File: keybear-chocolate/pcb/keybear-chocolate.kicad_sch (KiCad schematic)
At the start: 102 parts, among them J1 MJ-4PP-9, J2 BATT, J3 LED, J4 OLED, SW1 SW_PUSH, SW10 SW_PUSH, SW11 SW_PUSH, SW12 SW_PUSH, SW13 SW_PUSH, SW14 SW_PUSH, SW15 SW_PUSH, SW16 SW_PUSH, SW17 SW_PUSH, SW18 SW_PUSH, SW19 SW_PUSH, SW2 SW_PUSH, SW20 SW_PUSH, SW21 SW_PUSH, SW22 SW_PUSH, SW25 Rotary_Encoder_Switch, SW3 SW_PUSH, SW30 BATT_SW, SW4 SW_PUSH, SW5 SW_PUSH, SW6 SW_PUSH, SW7 SW_PUSH, SW8 SW_PUSH, SW9 SW_PUSH, U1 ProMicro

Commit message: usb-c added - WIP
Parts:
- added P1: USB_C_Plug, Connector_USB:USB_C_Receptacle_G-Switch_GT-USB-7010ASV, symbol Connector:USB_C_Receptacle
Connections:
- net GND: now also P1.A1 (GND), P1.A12 (GND), P1.B1 (GND), P1.B12 (GND)
- net VCC: now also P1.A4 (VBUS), P1.A9 (VBUS), P1.B4 (VBUS), P1.B9 (VBUS)
- net at J1.B, JP12.2, JP14.2: now also P1.A7 (D-), P1.B7 (D-)
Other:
- moved on the sheet: J1, J3, JP12, JP13, L1, L10, L11, L12, L13, L14, L15, L16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

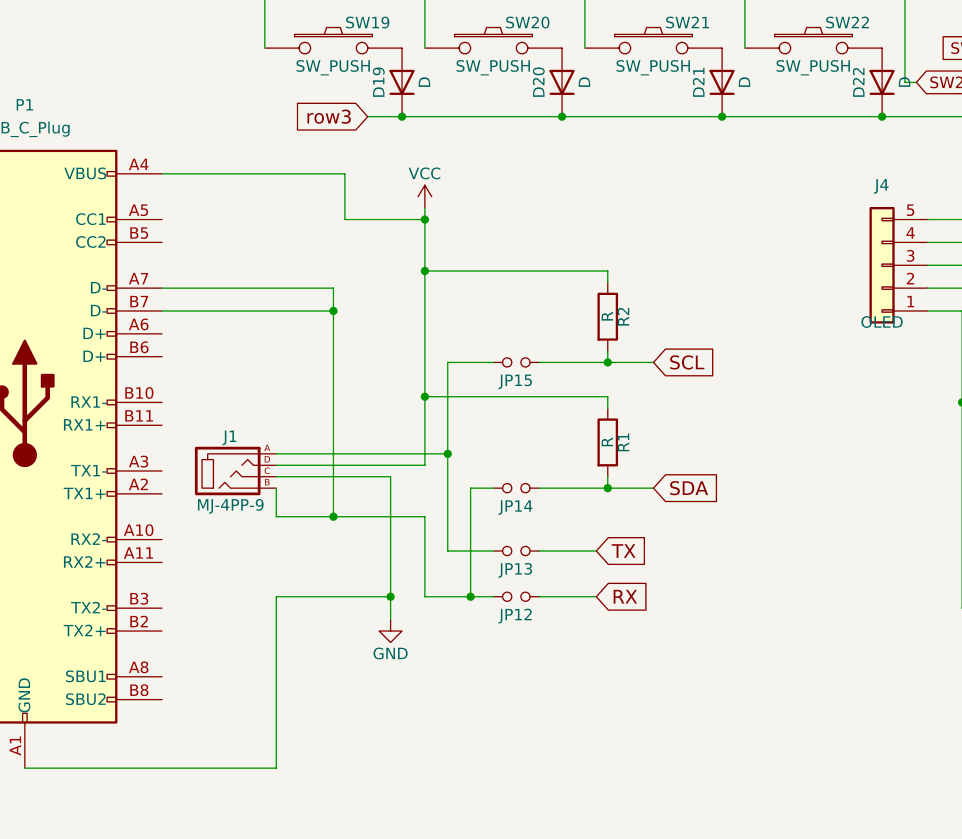
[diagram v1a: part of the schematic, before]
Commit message: usb-c rx-tx connections added
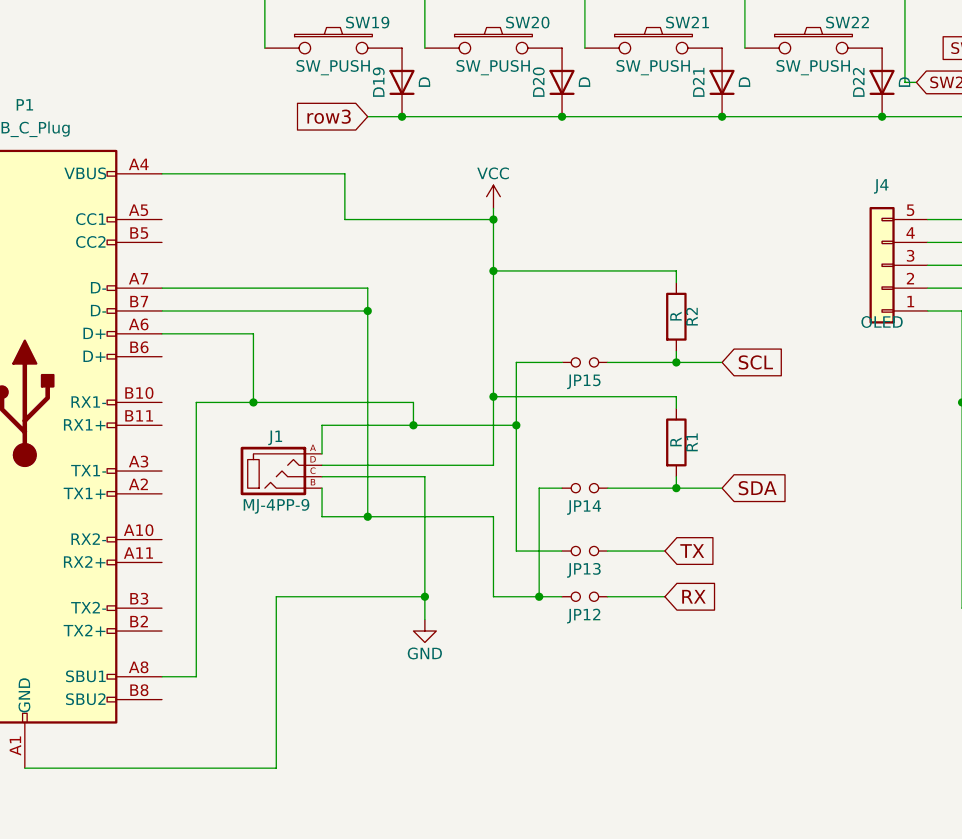
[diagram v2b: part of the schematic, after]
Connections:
- net at J1.A, JP13.2, JP15.2: now also P1.A6 (D+), P1.A8 (SBU1)
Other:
- moved on the sheet: J1, JP12, JP13, JP14, JP15, R1, R2

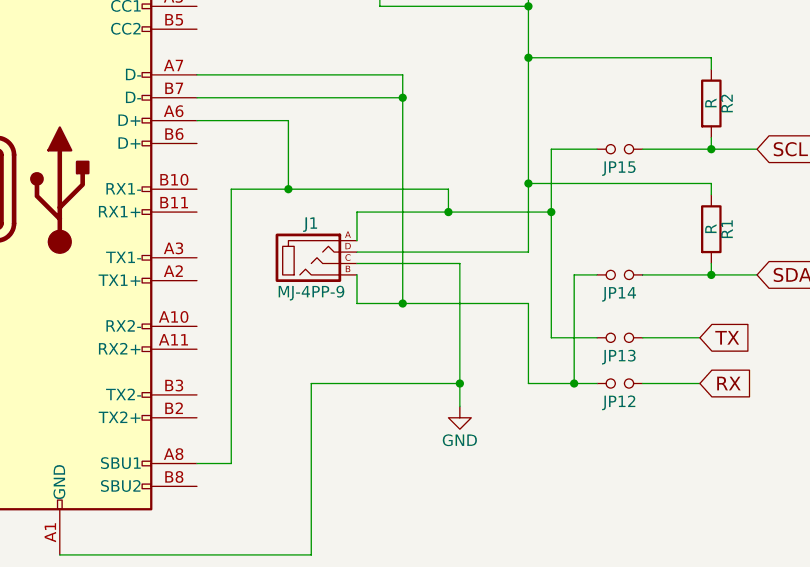
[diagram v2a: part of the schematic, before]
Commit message: trrs deleted. usb-c connected - v0.5
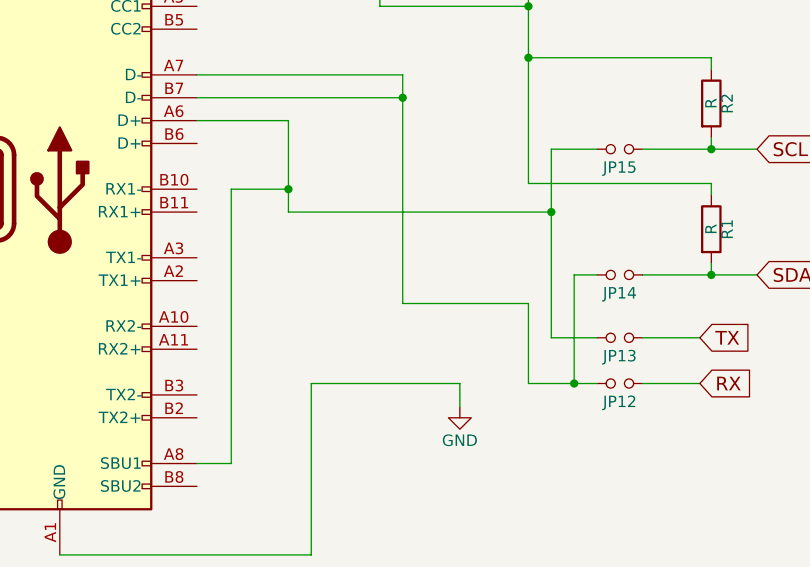
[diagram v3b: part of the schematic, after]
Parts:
- removed J1: MJ-4PP-9, kbd:MJ-4PP-9, symbol corne-chocolate-rescue:MJ-4PP-9-kbd
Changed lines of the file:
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@@
   (junction (at 232.41 58.42) (diameter 0) (color 0 0 0 0)
   )
-  (junction (at 181.61 157.48) (diameter 0) (color 0 0 0 0)
-  )
   (junction (at 217.17 81.28) (diameter 0) (color 0 0 0 0)
   )
@@
   (junction (at 49.53 167.64) (diameter 0) (color 0 0 0 0)
   )
-  (junction (at 180.34 138.43) (diameter 0) (color 0 0 0 0)
-  )
   (junction (at 34.29 172.72) (diameter 0) (color 0 0 0 0)
   )
-  (junction (at 175.26 148.59) (diameter 0) (color 0 0 0 0)
-  )
   (junction (at 234.95 66.04) (diameter 0) (color 0 0 0 0)
   )
@@
   (junction (at 250.19 73.66) (diameter 0) (color 0 0 0 0)
   )
-  (junction (at 189.23 135.255) (diameter 0) (color 0 0 0 0)
-  )
   (junction (at 64.77 172.72) (diameter 0) (color 0 0 0 0)
   )
@@
   (no_connect (at 121.92 64.77))
   (no_connect (at 31.75 172.72))
-  (wire (pts (xy 170.18 138.43) (xy 180.34 138.43))
-    (stroke (width 0) (type default))
-  )
   (wire (pts (xy 217.17 66.04) (xy 217.17 81.28))
     (stroke (width 0) (type default))
@@
     (stroke (width 0) (type default))
   )
-  (wire (pts (xy 170.18 138.43) (xy 170.18 141.605))
-    (stroke (width 0) (type default))
-  )
   (wire (pts (xy 209.55 144.145) (xy 209.55 145.415))
     (stroke (width 0) (type default))
@@
     (stroke (width 0) (type default))
   )
-  (wire (pts (xy 180.34 138.43) (xy 191.77 138.43))
-    (stroke (width 0) (type default))
-  )
   (wire (pts (xy 110.49 167.64) (xy 110.49 180.34))
     (stroke (width 0) (type default))
@@
     (stroke (width 0) (type default))
   )
-  (wire (pts (xy 170.18 144.145) (xy 181.61 144.145))
-    (stroke (width 0) (type default))
-  )
   (wire (pts (xy 242.57 123.19) (xy 237.49 123.19))
     (stroke (width 0) (type default))
@@
     (stroke (width 0) (type default))
   )
-  (wire (pts (xy 170.18 142.875) (xy 189.23 142.875))
-    (stroke (width 0) (type default))
-  )
   (wire (pts (xy 194.31 145.415) (xy 194.31 157.48))
     (stroke (width 0) (type default))
@@
     (stroke (width 0) (type default))
   )
-  (wire (pts (xy 180.34 135.89) (xy 180.34 138.43))
-    (stroke (width 0) (type default))
-  )
   (wire (pts (xy 80.01 154.94) (xy 80.01 160.02))
     (stroke (width 0) (type default))
@@
     (stroke (width 0) (type default))
   )
-  (wire (pts (xy 170.18 148.59) (xy 170.18 145.415))
+  (wire (pts (xy 62.23 189.23) (xy 46.99 189.23))
     (stroke (width 0) (type default))
   )
-  (wire (pts (xy 62.23 189.23) (xy 46.99 189.23))
+  (wire (pts (xy 162.56 138.43) (xy 162.56 135.89))
     (stroke (width 0) (type default))
   )
@@
     (stroke (width 0) (type default))
   )
-  (wire (pts (xy 162.56 135.89) (xy 180.34 135.89))
+  (wire (pts (xy 162.56 138.43) (xy 191.77 138.43))
     (stroke (width 0) (type default))
   )
@@
     (stroke (width 0) (type default))
   )
-  (wire (pts (xy 175.26 148.59) (xy 170.18 148.59))
-    (stroke (width 0) (type default))
-  )
   (wire (pts (xy 20.955 109.855) (xy 29.21 109.855))
     (stroke (width 0) (type default))
@@
     (stroke (width 0) (type default))
   )
-  (wire (pts (xy 181.61 144.145) (xy 181.61 157.48))
-    (stroke (width 0) (type default))
-  )
   (wire (pts (xy 49.53 142.24) (xy 49.53 147.32))
     (stroke (width 0) (type default))
@@
     (stroke (width 0) (type default))
   )
-  (wire (pts (xy 189.23 142.875) (xy 189.23 135.255))
-    (stroke (width 0) (type default))
-  )
   (wire (pts (xy 62.23 180.34) (xy 64.77 180.34))
     (stroke (width 0) (type default))
@@
         )
       )
-    )
-  )
-  (symbol (lib_id "corne-chocolate-rescue:MJ-4PP-9-kbd") (at 165.1 143.51 0) (unit 1)
-    (in_bom yes) (on_board yes) (dnp no)
-    (property "Reference" "J1" (at 165.1 139.7 0)
-      (effects (font (size 1.27 1.27)))
-    )
-    (property "Value" "MJ-4PP-9" (at 165.1 147.32 0)
-      (effects (font (size 1.27 1.27)))
-    )
-    (property "Footprint" "kbd:MJ-4PP-9" (at 172.085 139.065 0)
-      (effects (font (size 1.27 1.27)) hide)
-    )
-    (property "Datasheet" "" (at 172.085 139.065 0)
-      (effects (font (size 1.27 1.27)) hide)
-    )
-    (pin "A")
-    (pin "B")
-    (pin "C")
-    (pin "D")
-    (instances
-      (project "keybear-chocolate"
-        (path "/b2404ab0-025a-473e-9fbb-0abc932972cf"
-          (reference "J1") (unit 1)
-        )
-      )

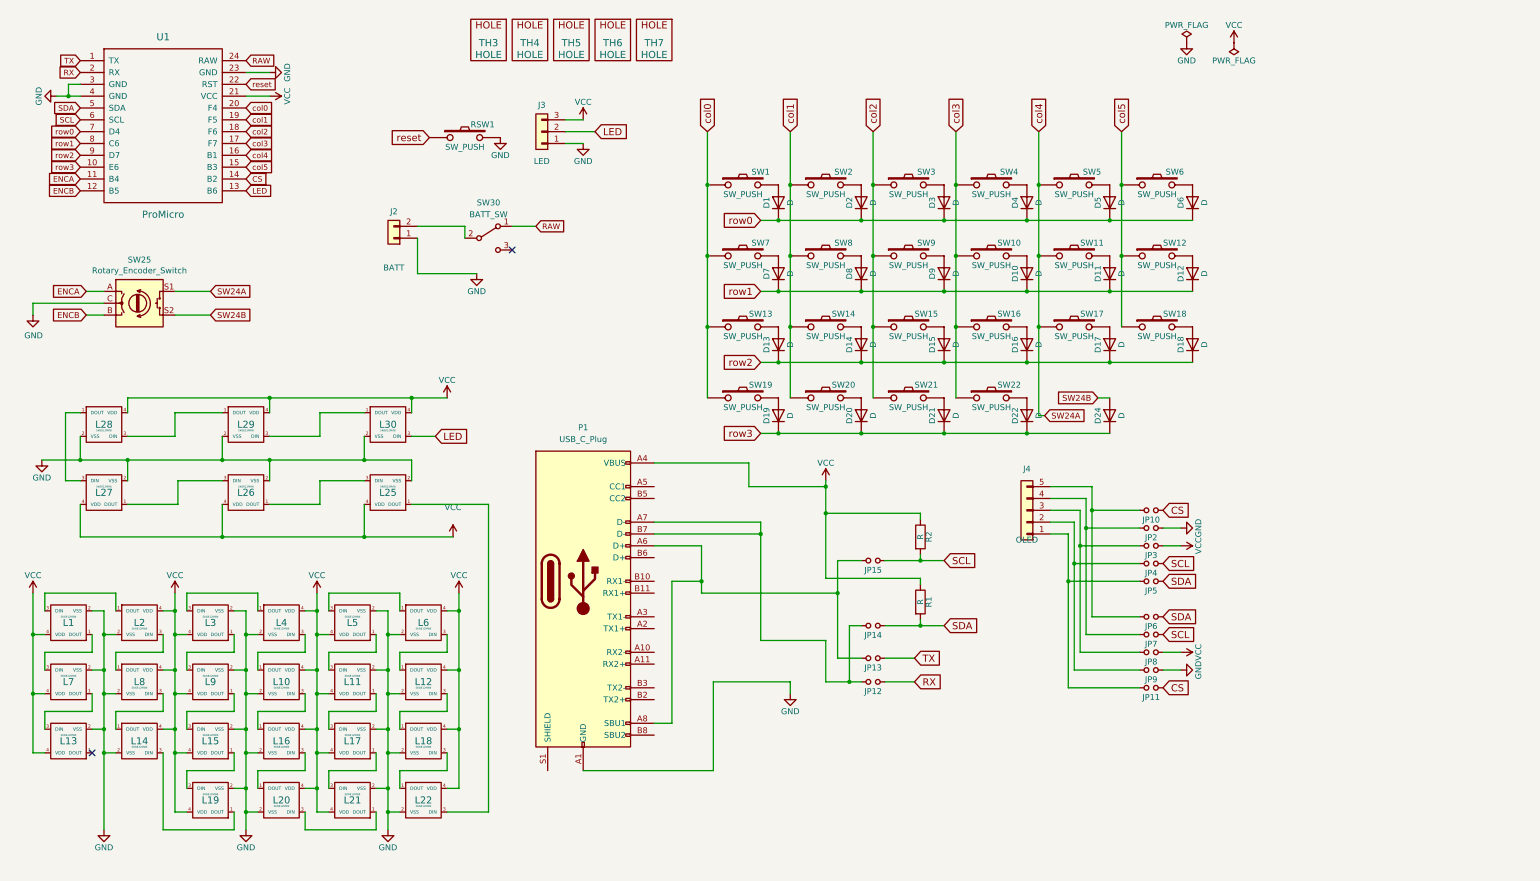
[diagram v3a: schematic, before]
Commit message: adding MPC23P17_ML to add the external GPIO pins
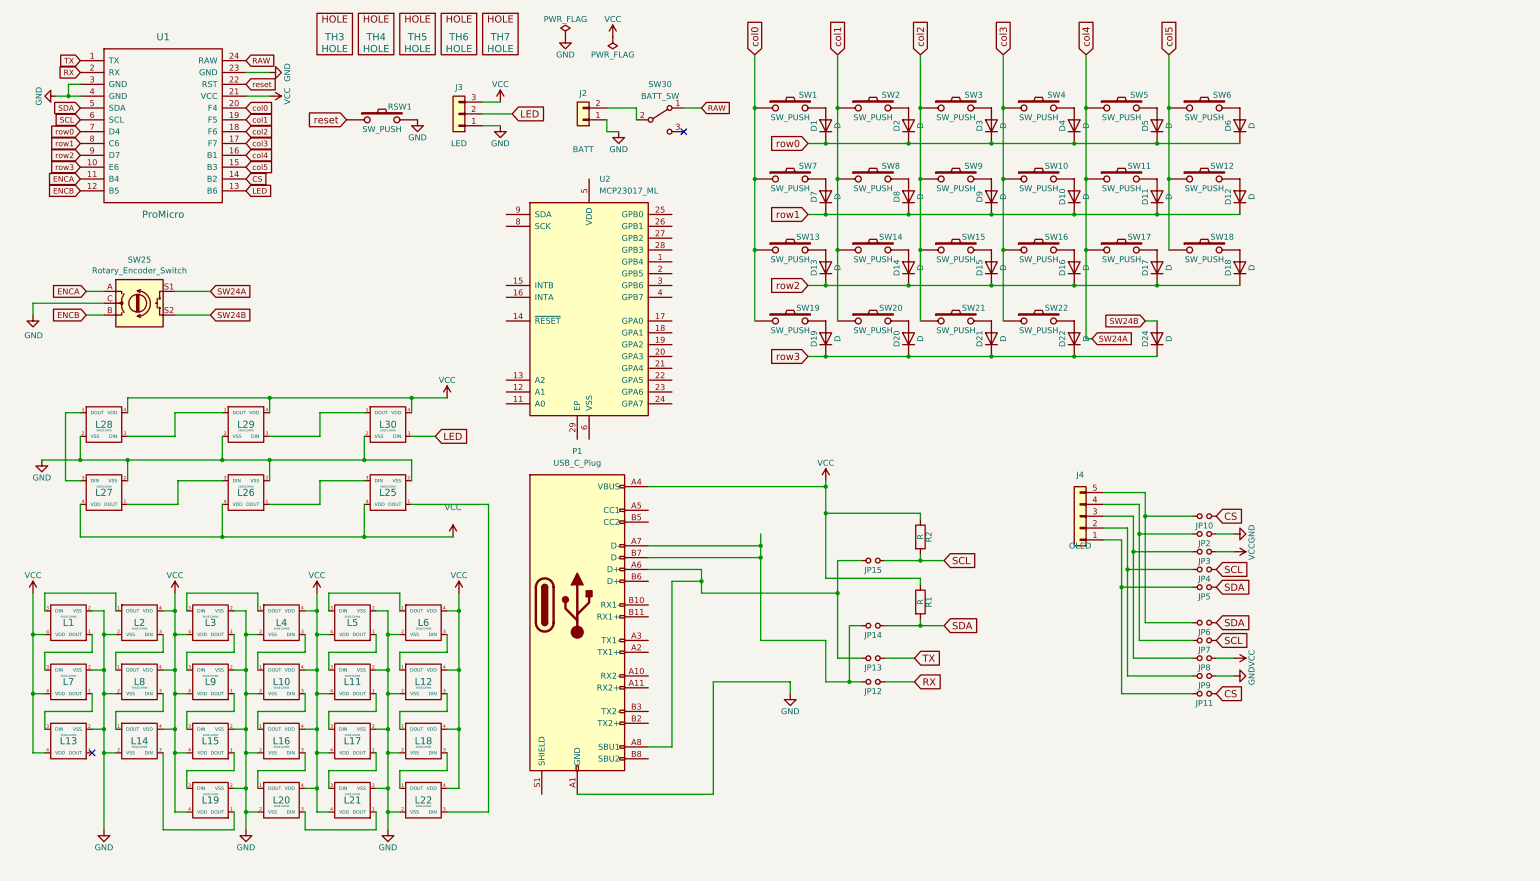
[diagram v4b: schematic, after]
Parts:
- added U2: MCP23017_ML, Package_DFN_QFN:QFN-28-1EP_6x6mm_P0.65mm_EP4.25x4.25mm, symbol Interface_Expansion:MCP23017_ML
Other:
- moved on the sheet: D1, D10, D11, D12, D13, D14, D15, D16, D17, D18, D19, D2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

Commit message: connecting MPC23P17_ML
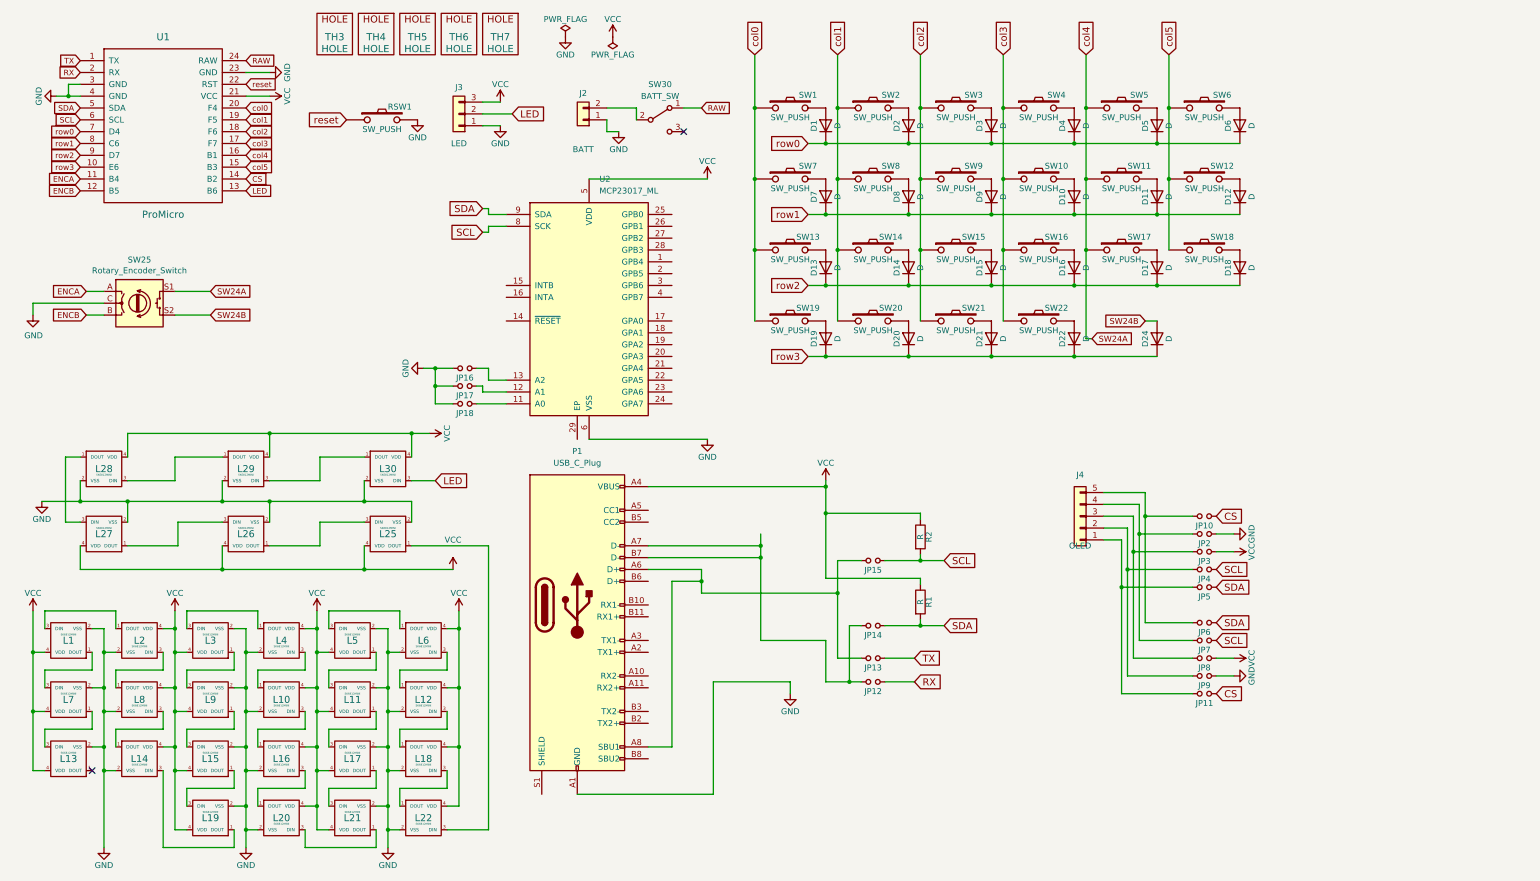
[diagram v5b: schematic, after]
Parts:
- added JP16, JP17, JP18: (no value), kbd:Jumper, symbol corne-chocolate-rescue:Jumper_NO_Small-Device
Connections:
- net GND: now also U2.6 (VSS), JP16.2, JP17.2, JP18.2
- net SCL: now also U2.8 (SCK)
- net SDA: now also U2.9 (SDA)
- net VCC: now also U2.5 (VDD)
- net at U2.11 (A0): now also JP18.1
- net at U2.12 (A1): now also JP17.1
- net at U2.13 (A2): now also JP16.1
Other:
- moved on the sheet: L1, L10, L11, L12, L13, L14, L15, L16, L17, L18, L19, L2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

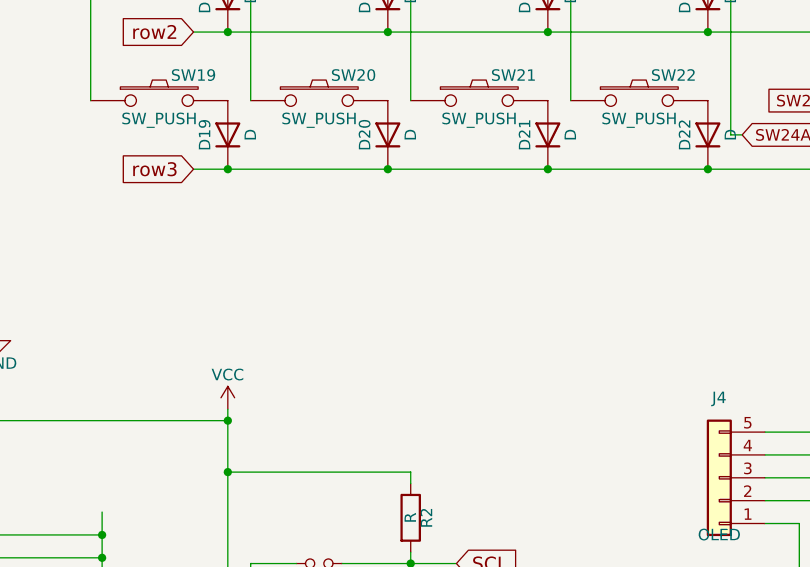
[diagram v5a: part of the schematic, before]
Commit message: adding ATECC608A-SSHDA crypto chip
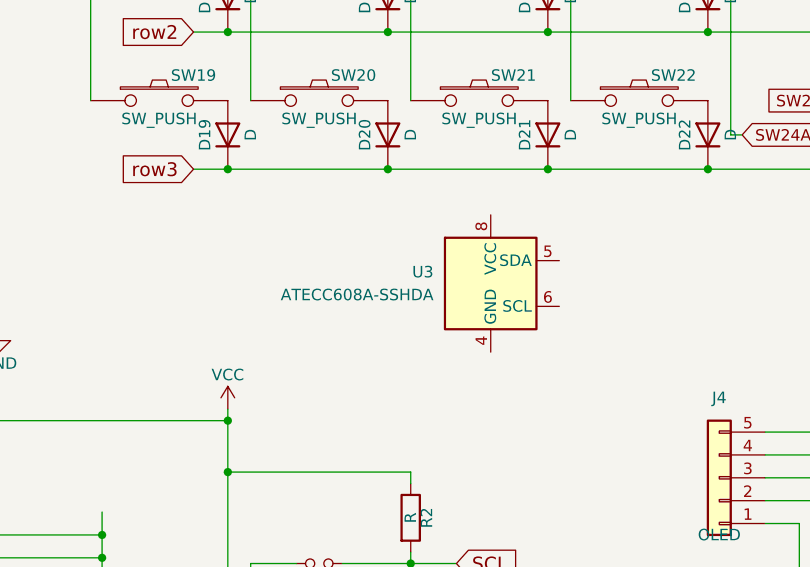
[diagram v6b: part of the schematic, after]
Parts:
- added U3: ATECC608A-SSHDA, Package_SO:SOIC-8_3.9x4.9mm_P1.27mm, symbol Security:ATECC608A-SSHDA
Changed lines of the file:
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@@
+    )
+  )
+  (symbol (lib_id "Security:ATECC608A-SSHDA") (at 218.44 100.33 0) (unit 1)
+    (in_bom yes) (on_board yes) (dnp no) (fields_autoplaced)
+    (property "Reference" "U3" (at 212.09 99.06 0)
+      (effects (font (size 1.27 1.27)) (justify right))
+    )
+    (property "Value" "ATECC608A-SSHDA" (at 212.09 101.6 0)
+      (effects (font (size 1.27 1.27)) (justify right))
+    )
+    (property "Footprint" "Package_SO:SOIC-8_3.9x4.9mm_P1.27mm" (at 218.44 100.33 0)
+      (effects (font (size 1.27 1.27)) hide)
+    )
+    (property "Datasheet" "http://ww1.microchip.com/downloads/en/DeviceDoc/ATECC608A-CryptoAuthentication-Device-Summary-Data-Sheet-DS40001977B.pdf" (at 222.25 93.98 0)
+      (effects (font (size 1.27 1.27)) hide)
+    )
+    (pin "1")
+    (pin "2")
+    (pin "3")
+    (pin "4")
+    (pin "5")
+    (pin "6")
+    (pin "7")
+    (pin "8")
+    (instances
+      (project "keybear-chocolate"
+        (path "/b2404ab0-025a-473e-9fbb-0abc932972cf"
+          (reference "U3") (unit 1)
+        )
+      )
     )
   )
